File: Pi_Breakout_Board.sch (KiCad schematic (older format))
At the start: 70 parts, among them J1 Raspberry_Pi_2_3, J2 Conn_02x04_Odd_Even heater he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, J3 Conn_02x08_Odd_Even thermisto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, J4 Screw_Terminal_01x02, J5 Conn_01x08_Male, J6 Conn_01x08_Male, J7 Conn_01x05_Male uart breakout, Q1 Q_NMOS_GDSD, Q2 Q_NMOS_GDSD, Q3 Q_NMOS_GDSD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

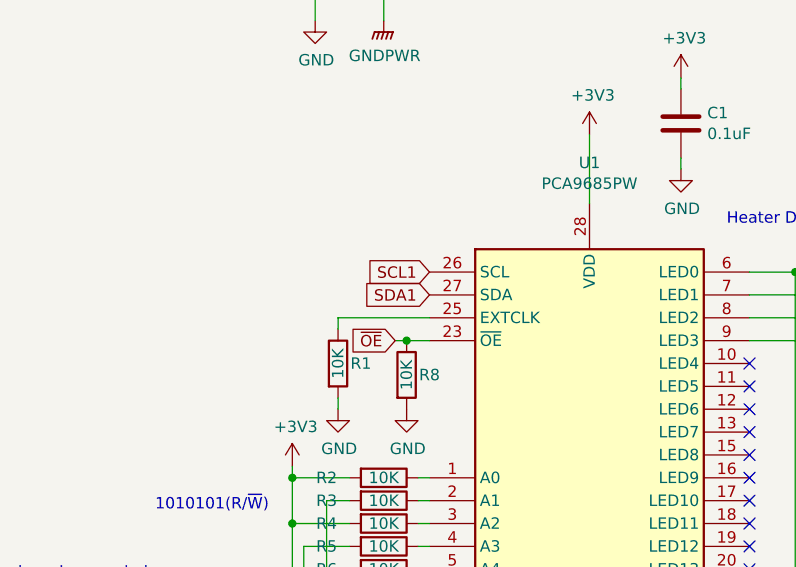
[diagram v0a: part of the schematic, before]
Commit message: move the PCA9865 from I2C1 to I2C0. Routing saga continues
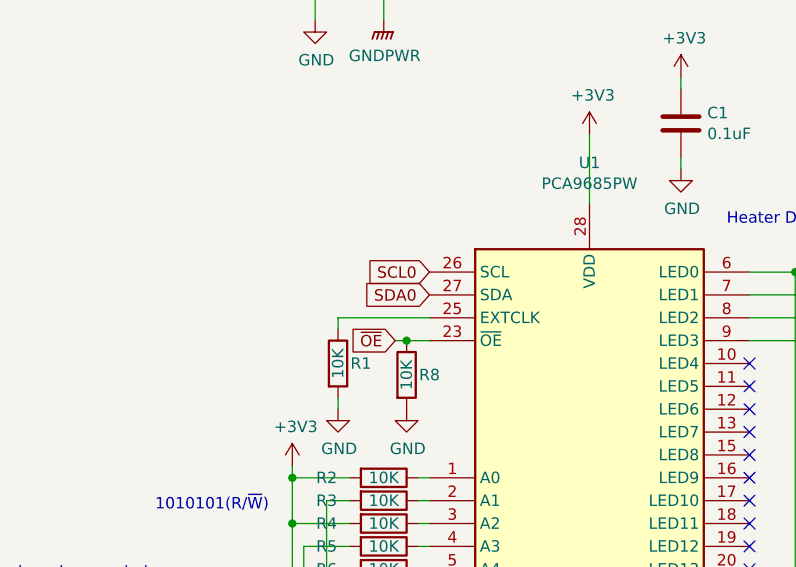
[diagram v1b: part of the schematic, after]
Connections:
- net SCL0: now also U1.26 (SCL)
- net SCL1: no longer U1.26 (SCL)
- net SDA0: now also U1.27 (SDA)
- net SDA1: no longer U1.27 (SDA)
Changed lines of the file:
@@
 	4350 7550 4250 7550
 Text GLabel 2450 5550 0    50   Input ~ 0
-SDA1
+SDA0
 Text GLabel 2450 5450 0    50   Input ~ 0
-SCL1
+SCL0
 $Comp
 L Device:R R9

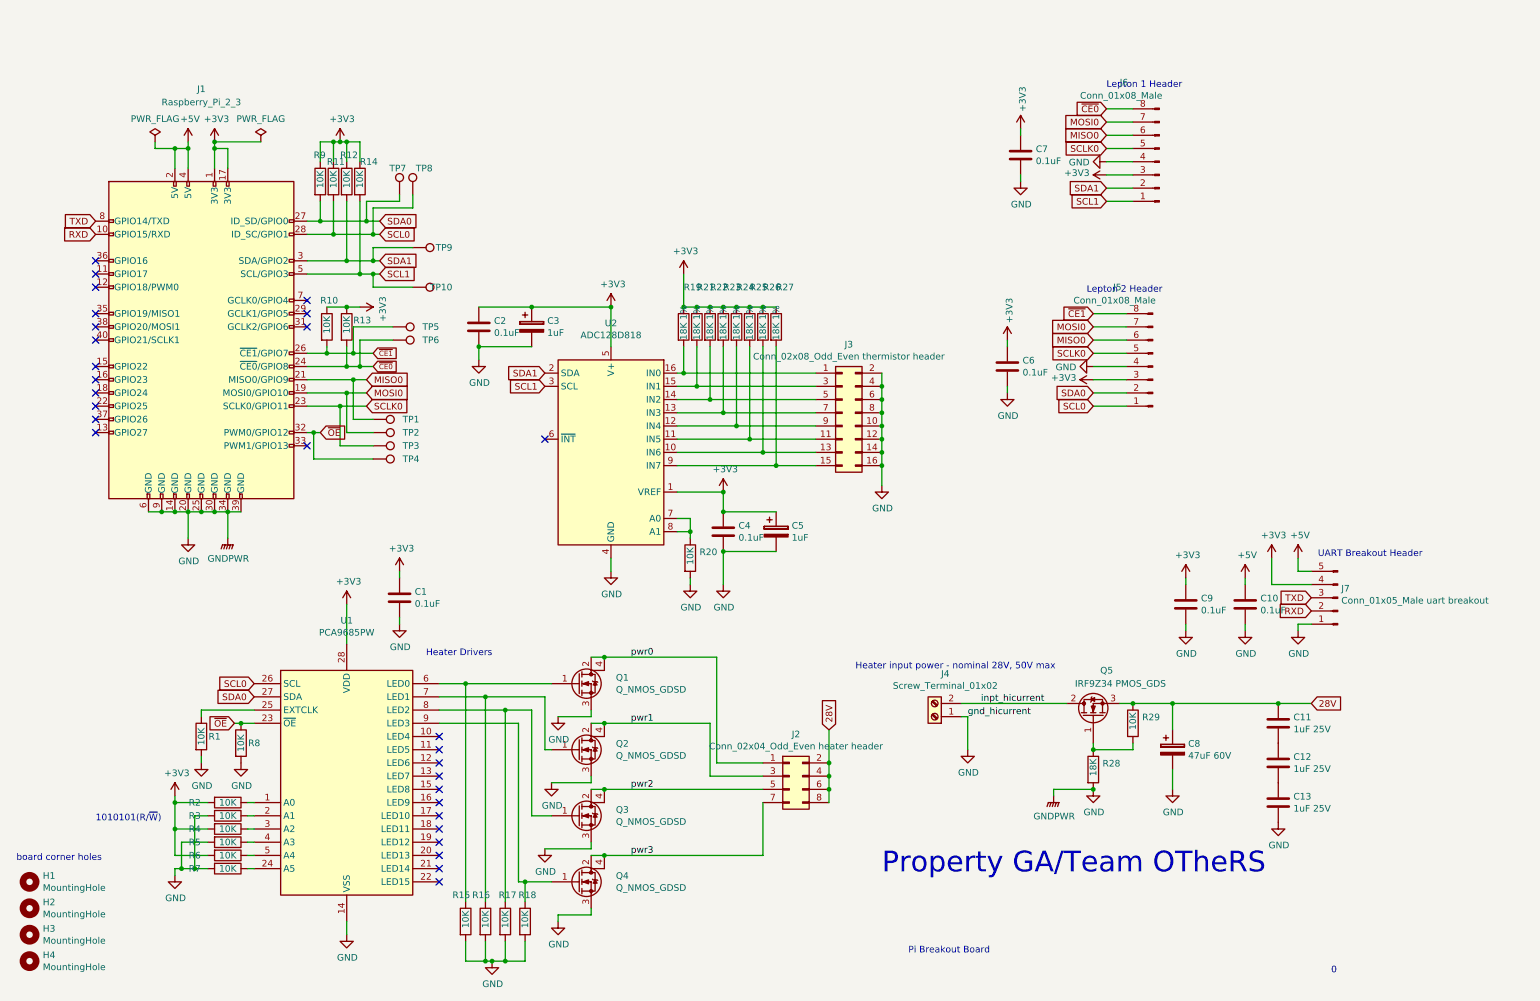
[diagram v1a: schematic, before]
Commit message: rev3 with corrected header placement in work
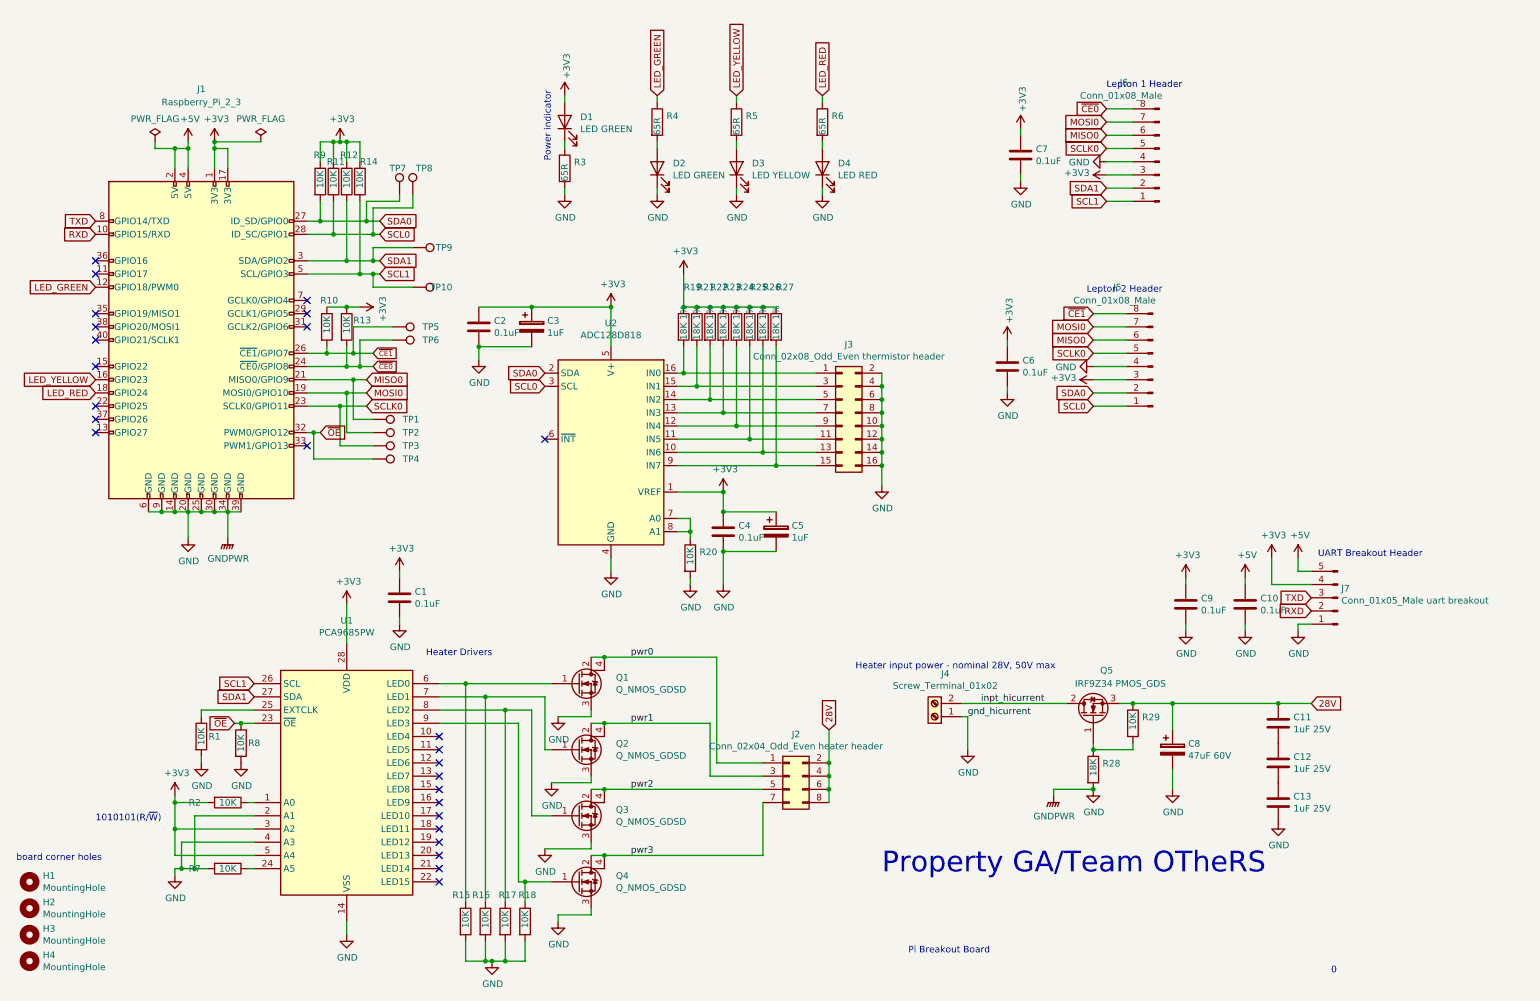
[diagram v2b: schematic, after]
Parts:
- added D1, D2: LED GREEN, LED_SMD:LED_0805_2012Metric_Pad1.15x1.40mm_HandSolder, symbol Device:LED
- added D3: LED YELLOW, LED_SMD:LED_0805_2012Metric_Pad1.15x1.40mm_HandSolder, symbol Device:LED
- added D4: LED RED, LED_SMD:LED_0805_2012Metric_Pad1.15x1.40mm_HandSolder, symbol Device:LED
- R3, R4, R5, R6: value 10K -> 65R; footprint Resistor_SMD:R_1206_3216Metric_Pad1.42x1.75mm_HandSolder -> Resistor_SMD:R_0805_2012Metric_Pad1.15x1.40mm_HandSolder
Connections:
- net +3V3: now also U1.3 (A2), U1.5 (A4), D1.2 (A); no longer R4.2, R6.2
- net GND: now also U1.2 (A1), U1.4 (A3), D2.1 (K), D3.1 (K), D4.1 (K); no longer R5.2
- net SCL0: now also U2.3 (SCL); no longer U1.26 (SCL)
- net SCL1: now also U1.26 (SCL); no longer U2.3 (SCL)
- net SDA0: now also U2.2 (SDA); no longer U1.27 (SDA)
- net SDA1: now also U1.27 (SDA); no longer U2.2 (SDA)
- net LED_GREEN: now reaches J1.12 (GPIO18/PWM0)
- net LED_GREEN: now also R4.1
- net LED_YELLOW: now reaches J1.16 (GPIO23)
- net LED_YELLOW: now also R5.1
- net LED_RED: now reaches J1.18 (GPIO24)
- net LED_RED: now also R6.1
- net at R3.1: now also D1.1 (K); no longer U1.2 (A1)
- new net: D2.2 (A), R4.2
- new net: D3.2 (A), R5.2
- new net: D4.2 (A), R6.2
- no-connect marks 29 -> 26
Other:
- note added: "Power indicator"
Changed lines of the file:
@@
 $EndDescr
-$Comp
-L Connector:Raspberry_Pi_2_3 J1
-U 1 1 5C3DFC77
-P 2050 2850
-F 0 "J1" H 2050 4750 50  0000 C CNN
-F 1 "Raspberry_Pi_2_3" H 2050 4650 50  0000 C CNN
-F 2 "Connector_PinHeader_2.54mm:PinHeader_2x20_P2.54mm_Vertical" H 2050 2850 50  0001 C CNN
-F 3 "https://www.raspberrypi.org/documentation/hardware/raspberrypi/schematics/rpi_SCH_3bplus_1p0_reduced.pdf" H 2050 2850 50  0001 C CNN
-	1    2050 2850
-	1    0    0    -1
-$EndComp
 $Comp
 L power:+3V3 #PWR06
@@
 	1    0    0    -1
 $EndComp
-Wire Wire Line
-	1850 4150 1950 4150
 Connection ~ 1950 4150
-Connection ~ 2150 4150
-Wire Wire Line
-	2150 4150 2250 4150
 Connection ~ 2250 4150
 Wire Wire Line
@@
 	4350 7550 4250 7550
 Text GLabel 2450 5550 0    50   Input ~ 0
-SDA0
+SDA1
 Text GLabel 2450 5450 0    50   Input ~ 0
-SCL0
+SCL1
 $Comp
 L Device:R R9
@@
 $EndComp
 Text GLabel 4650 3200 0    50   Input ~ 0
-SCL1
+SCL0
 Text GLabel 4650 3100 0    50   Input ~ 0
-SDA1
+SDA0
 $Comp
 L Connector_Generic:Conn_02x08_Odd_Even J3
@@
 $EndComp
 $Comp
-L Device:R R6
-U 1 1 5C596E06
-P 2250 6750
-F 0 "R6" V 2250 6500 50  0000 C CNN
-F 1 "10K" V 2250 6750 50  0000 C CNN
-F 2 "Resistor_SMD:R_1206_3216Metric_Pad1.42x1.75mm_HandSolder" V 2180 6750 50  0001 C CNN
-F 3 "~" H 2250 6750 50  0001 C CNN
-	1    2250 6750
-	0    1    1    0
-$EndComp
-$Comp
-L Device:R R5
-U 1 1 5C596EA0
-P 2250 6650
-F 0 "R5" V 2250 6400 50  0000 C CNN
-F 1 "10K" V 2250 6650 50  0000 C CNN
-F 2 "Resistor_SMD:R_1206_3216Metric_Pad1.42x1.75mm_HandSolder" V 2180 6650 50  0001 C CNN
-F 3 "~" H 2250 6650 50  0001 C CNN
-	1    2250 6650
-	0    1    1    0
-$EndComp
-$Comp
-L Device:R R4
-U 1 1 5C596F44
-P 2250 6550
-F 0 "R4" V 2250 6300 50  0000 C CNN
-F 1 "10K" V 2250 6550 50  0000 C CNN
-F 2 "Resistor_SMD:R_1206_3216Metric_Pad1.42x1.75mm_HandSolder" V 2180 6550 50  0001 C CNN
-F 3 "~" H 2250 6550 50  0001 C CNN
-	1    2250 6550
-	0    1    1    0
-$EndComp
-$Comp
-L Device:R R3
-U 1 1 5C596FE2
-P 2250 6450
-F 0 "R3" V 2250 6200 50  0000 C CNN
-F 1 "10K" V 2250 6450 50  0000 C CNN
-F 2 "Resistor_SMD:R_1206_3216Metric_Pad1.42x1.75mm_HandSolder" V 2180 6450 50  0001 C CNN
-F 3 "~" H 2250 6450 50  0001 C CNN
-	1    2250 6450
-	0    1    1    0
-$EndComp
-$Comp
 L Device:R R2
 U 1 1 5C597086
@@
 $EndComp
 Wire Wire Line
-	2400 6450 2450 6450
-Wire Wire Line
-	2450 6550 2400 6550
-Wire Wire Line
-	2400 6650 2450 6650
-Wire Wire Line
-	2450 6750 2400 6750
-Wire Wire Line
 	2400 6850 2450 6850
 Text Notes 1250 6500 0    50   ~ 0
@@
 	2300 5750 2350 5750
 Connection ~ 2350 5750
-NoConn ~ 1250 2250
 NoConn ~ 1250 2350
-NoConn ~ 1250 2450
 NoConn ~ 1250 2650
-NoConn ~ 1250 2750
-NoConn ~ 1250 2850
 NoConn ~ 1250 3050
-NoConn ~ 1250 3150
-NoConn ~ 1250 3250
-Connection ~ 1850 4150
-Connection ~ 2050 4150
-Wire Wire Line
-	2050 4150 2150 4150
-Wire Wire Line
-	1950 4150 2050 4150
-Connection ~ 1750 4150
-Wire Wire Line
-	1750 4150 1850 4150
-Wire Wire Line
-	1650 4150 1750 4150
 NoConn ~ 1250 3350
 NoConn ~ 1250 3450
@@
 Wire Wire Line
 	1850 6350 1850 6550
-Wire Wire Line
-	1850 6750 2100 6750
 Connection ~ 1850 6350
-Wire Wire Line
-	2100 6650 1900 6650
 Wire Wire Line
 	1900 6650 1900 6850
@@
 Wire Wire Line
 	1900 6850 1850 6850
-Wire Wire Line
-	2100 6550 1850 6550
 Connection ~ 1850 6550
 Wire Wire Line
@@
 Wire Wire Line
 	2000 6450 2000 6850
-Wire Wire Line
-	2000 6450 2100 6450
 Connection ~ 2000 6850
 Wire Wire Line
@@
 Wire Wire Line
 	3000 2950 2850 2950
+Wire Wire Line
+	2000 6450 2450 6450
+Wire Wire Line
+	1850 6550 2450 6550
+Wire Wire Line
+	1900 6650 2450 6650
+Wire Wire Line
+	1850 6750 2450 6750
+$Comp
+L Device:LED D1
+U 1 1 5C800D86
+P 4800 1200
+F 0 "D1" V 4838 1082 50  0000 R CNN
+F 1 "LED GREEN" V 4747 1082 50  0000 R CNN
+F 2 "LED_SMD:LED_0805_2012Metric_Pad1.15x1.40mm_HandSolder" H 4800 1200 50  0001 C CNN
+F 3 "~" H 4800 1200 50  0001 C CNN
+	1    4800 1200
+	0    -1   -1   0
+$EndComp
+$Comp
+L power:+3V3 #PWR048
+U 1 1 5C801487
+P 4800 1000
+F 0 "#PWR048" H 4800 850 50  0001 C CNN
+F 1 "+3V3" V 4815 1128 50  0000 L CNN
+F 2 "" H 4800 1000 50  0001 C CNN
+F 3 "" H 4800 1000 50  0001 C CNN
+	1    4800 1000
+	1    0    0    -1
+$EndComp
+$Comp
+L Device:R R3
+U 1 1 5C801580
+P 4800 1550
+F 0 "R3" H 4870 1596 50  0000 L CNN
+F 1 "65R" V 4800 1450 50  0000 L CNN
+F 2 "Resistor_SMD:R_0805_2012Metric_Pad1.15x1.40mm_HandSolder" V 4730 1550 50  0001 C CNN
+F 3 "~" H 4800 1550 50  0001 C CNN
+	1    4800 1550
+	1    0    0    -1
+$EndComp
+$Comp
+L power:GND #PWR049
+U 1 1 5C80164A
+P 4800 1750
+F 0 "#PWR049" H 4800 1500 50  0001 C CNN
+F 1 "GND" H 4805 1577 50  0000 C CNN
+F 2 "" H 4800 1750 50  0001 C CNN
+F 3 "" H 4800 1750 50  0001 C CNN
+	1    4800 1750
+	1    0    0    -1
+$EndComp
+Wire Wire Line
+	4800 1000 4800 1050
+Wire Wire Line
+	4800 1350 4800 1400
+Wire Wire Line
+	4800 1700 4800 1750
+Text GLabel 1250 2450 0    50   Input ~ 0
+LED_GREEN
+Wire Wire Line
+	1650 4150 1750 4150
+Connection ~ 1750 4150
+Wire Wire Line
+	2150 4150 2250 4150
+Connection ~ 2150 4150
+Wire Wire Line
+	1950 4150 2050 4150
+Wire Wire Line
+	2050 4150 2150 4150
+Connection ~ 2050 4150
+Wire Wire Line
+	1750 4150 1850 4150
+Wire Wire Line
+	1850 4150 1950 4150
+Connection ~ 1850 4150
+$Comp
+L Connector:Raspberry_Pi_2_3 J1
+U 1 1 5C3DFC77
+P 2050 2850
+F 0 "J1" H 2050 4750 50  0000 C CNN
+F 1 "Raspberry_Pi_2_3" H 2050 4650 50  0000 C CNN
+F 2 "Connector_PinHeader_2.54mm:PinHeader_2x20_P2.54mm_Vertical" H 2050 2850 50  0001 C CNN
+F 3 "https://www.raspberrypi.org/documentation/hardware/raspberrypi/schematics/rpi_SCH_3bplus_1p0_reduced.pdf" H 2050 2850 50  0001 C CNN
+	1    2050 2850
+	1    0    0    -1
+$EndComp
+Text GLabel 1250 3150 0    50   Input ~ 0
+LED_YELLOW
+Text GLabel 1250 3250 0    50   Input ~ 0
+LED_RED
+$Comp
+L Device:LED D2
+U 1 1 5C854E19
+P 5500 1550
+F 0 "D2" V 5538 1432 50  0000 R CNN
+F 1 "LED GREEN" V 5447 1432 50  0000 R CNN
+F 2 "LED_SMD:LED_0805_2012Metric_Pad1.15x1.40mm_HandSolder" H 5500 1550 50  0001 C CNN
+F 3 "~" H 5500 1550 50  0001 C CNN
+	1    5500 1550
+	0    -1   -1   0
+$EndComp
+$Comp
+L power:GND #PWR050
+U 1 1 5C854E2D
+P 5500 1750
+F 0 "#PWR050" H 5500 1500 50  0001 C CNN
+F 1 "GND" H 5505 1577 50  0000 C CNN
+F 2 "" H 5500 1750 50  0001 C CNN
+F 3 "" H 5500 1750 50  0001 C CNN
+	1    5500 1750
+	1    0    0    -1
+$EndComp
+Wire Wire Line
+	5500 1000 5500 1050
+Wire Wire Line
+	5500 1350 5500 1400
+Wire Wire Line
+	5500 1700 5500 1750
+$Comp
+L Device:LED D3
+U 1 1 5C8694C5
+P 6100 1550
+F 0 "D3" V 6138 1433 50  0000 R CNN
+F 1 "LED YELLOW" V 6047 1433 50  0000 R CNN
+F 2 "LED_SMD:LED_0805_2012Metric_Pad1.15x1.40mm_HandSolder" H 6100 1550 50  0001 C CNN
+F 3 "~" H 6100 1550 50  0001 C CNN
+	1    6100 1550
+	0    -1   -1   0
+$EndComp
+$Comp
+L power:GND #PWR051
+U 1 1 5C8694D9
+P 6100 1750
+F 0 "#PWR051" H 6100 1500 50  0001 C CNN
+F 1 "GND" H 6105 1577 50  0000 C CNN
+F 2 "" H 6100 1750 50  0001 C CNN
+F 3 "" H 6100 1750 50  0001 C CNN
+	1    6100 1750
+	1    0    0    -1
+$EndComp
+Wire Wire Line
+	6100 1000 6100 1050
+Wire Wire Line
+	6100 1350 6100 1400
+Wire Wire Line
+	6100 1700 6100 1750
+$Comp
+L Device:LED D4
+U 1 1 5C87E05E
+P 6750 1550
+F 0 "D4" V 6788 1432 50  0000 R CNN
+F 1 "LED RED" V 6697 1432 50  0000 R CNN
+F 2 "LED_SMD:LED_0805_2012Metric_Pad1.15x1.40mm_HandSolder" H 6750 1550 50  0001 C CNN
+F 3 "~" H 6750 1550 50  0001 C CNN
+	1    6750 1550
+	0    -1   -1   0
+$EndComp
+$Comp
+L power:GND #PWR052
+U 1 1 5C87E072
+P 6750 1750
+F 0 "#PWR052" H 6750 1500 50  0001 C CNN
+F 1 "GND" H 6755 1577 50  0000 C CNN
+F 2 "" H 6750 1750 50  0001 C CNN
+F 3 "" H 6750 1750 50  0001 C CNN
+	1    6750 1750
+	1    0    0    -1
+$EndComp
+Wire Wire Line
+	6750 1000 6750 1050
+Wire Wire Line
+	6750 1350 6750 1400
+Wire Wire Line
+	6750 1700 6750 1750
+Text GLabel 5500 1000 1    50   Input ~ 0
+LED_GREEN
+Text GLabel 6100 1000 1    50   Input ~ 0
+LED_YELLOW
+Text GLabel 6750 1000 1    50   Input ~ 0
+LED_RED
+Text Notes 4700 1500 1    50   ~ 0
+Power indicator
+$Comp
+L Device:R R4
+U 1 1 5C803FD8
+P 5500 1200
+F 0 "R4" H 5570 1246 50  0000 L CNN
+F 1 "65R" V 5500 1100 50  0000 L CNN
+F 2 "Resistor_SMD:R_0805_2012Metric_Pad1.15x1.40mm_HandSolder" V 5430 1200 50  0001 C CNN
+F 3 "~" H 5500 1200 50  0001 C CNN
+	1    5500 1200
+	1    0    0    -1
+$EndComp
+$Comp
+L Device:R R5
+U 1 1 5C80408C
+P 6100 1200
+F 0 "R5" H 6170 1246 50  0000 L CNN
+F 1 "65R" V 6100 1100 50  0000 L CNN
+F 2 "Resistor_SMD:R_0805_2012Metric_Pad1.15x1.40mm_HandSolder" V 6030 1200 50  0001 C CNN
+F 3 "~" H 6100 1200 50  0001 C CNN
+	1    6100 1200
+	1    0    0    -1
+$EndComp
+$Comp
+L Device:R R6
+U 1 1 5C8044FB
+P 6750 1200
+F 0 "R6" H 6820 1246 50  0000 L CNN
+F 1 "65R" V 6750 1100 50  0000 L CNN
+F 2 "Resistor_SMD:R_0805_2012Metric_Pad1.15x1.40mm_HandSolder" V 6680 1200 50  0001 C CNN
+F 3 "~" H 6750 1200 50  0001 C CNN
+	1    6750 1200
+	1    0    0    -1
+$EndComp
+NoConn ~ 1250 2850
+NoConn ~ 1250 2750
+NoConn ~ 1250 2250
 $EndSCHEMATC
